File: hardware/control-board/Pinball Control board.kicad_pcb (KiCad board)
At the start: 2 copper layers, 87.1 x 100 mm, 108 parts, among them J1 Connector C, J3 B4B-XH-A, J4 Conn_01x10_Pin, J5 Conn_01x10_Pin, Q1 BSS138, Q10 BSS84, Q11 BSS138, Q12 BSS84, Q13 BSS138, Q14 BSS84, Q15 BSS138, Q16 IRFR5410, Q17 IRFR5410, Q18 IRFR5410, Q19 IRFR5410, Q2 BSS138, Q20 IRFR5410, Q3 BSS138, Q4 BSS138, Q5 BSS138, Q6 BSS84, Q7 BSS138, Q8 BSS84, Q9 BSS138, SW1 test switch, SW2 test switch

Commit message: Save routed board checkpoint and order checklist
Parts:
- removed C22, C23: 100nF, PCM_JLCPCB:C_0805
- removed the D10 at (136.1, 62.6)
- removed the D15 at (146.3, 132.8)
- removed the D16 at (136.2, 135.0)
- removed the D9 at (146.8, 59.6)
- removed Q1, Q11, Q13, Q15, Q2, Q3, Q4, Q5, Q7, Q9: BSS138, PCM_JLCPCB:Q_SOT-23
- removed Q10, Q12, Q14, Q6, Q8: BSS84, PCM_JLCPCB:Q_SOT-23
- removed Q16, Q17, Q18, Q19, Q20: IRFR5410, Package_TO_SOT_SMD:TO-252-2
- removed the R20 at (157.2, 97.6)
- removed R25, R26, R27, R28: 56Ω, PCM_JLCPCB:R_0805
- removed R29, R30, R31, R32, R33: 10kΩ, PCM_JLCPCB:R_0805
- removed the R3 at (117.4, 121.1)
- removed R34, R37, R50, R51: 2.4kΩ, PCM_JLCPCB:R_0805
- added C17: 100nF, PCM_JLCPCB:C_0805, F.Cu at (151.9, 141.4)
- added C18: 100nF, PCM_JLCPCB:C_0805, F.Cu at (151.9, 86.8)
- added D13: Red, PCM_JLCPCB:D_0805, F.Cu at (146.7, 69.0)
- added D14: Red, PCM_JLCPCB:D_0805, F.Cu at (146.7, 105.4)
- added D19: US1M, PCM_JLCPCB:D_SMA, F.Cu at (149.1, 82.4)
- added D20: SMCJ30CA, PCM_JLCPCB:D_SMC, F.Cu at (139.0, 81.7)
- added R10: 220Ω, PCM_JLCPCB:R_0805, F.Cu at (154.6, 123.8)
- added R11: 220Ω, PCM_JLCPCB:R_0805, F.Cu at (154.5, 141.4)
- added R12: 220Ω, PCM_JLCPCB:R_0805, F.Cu at (154.5, 86.7)
- added R13: 220Ω, PCM_JLCPCB:R_0805, F.Cu at (157.1, 69.0)
- added R2: 4.7kΩ, PCM_JLCPCB:R_0805, F.Cu at (108.5, 118.0)
- added U1: TPS1H200AQDGNRQ1, Snapmagic_TI_TPS1H200A_Q1:SOP65P490X110-9N, F.Cu at (151.9, 115.4)
- added U2: TPS1H200AQDGNRQ1, Snapmagic_TI_TPS1H200A_Q1:SOP65P490X110-9N, F.Cu at (152.0, 132.9)
- added U3: TPS1H200AQDGNRQ1, Snapmagic_TI_TPS1H200A_Q1:SOP65P490X110-9N, F.Cu at (151.4, 78.0)
- added U4: TPS1H200AQDGNRQ1, Snapmagic_TI_TPS1H200A_Q1:SOP65P490X110-9N, F.Cu at (151.4, 60.4)
- added U5: TPS1H200AQDGNRQ1, Snapmagic_TI_TPS1H200A_Q1:SOP65P490X110-9N, F.Cu at (151.9, 96.5)
- D11: value US1M -> Red; footprint PCM_JLCPCB:D_SMA -> PCM_JLCPCB:D_0805
- D12: value SMCJ30CA -> Red; footprint PCM_JLCPCB:D_SMC -> PCM_JLCPCB:D_0805
- D21, D23: value Red -> US1M; footprint PCM_JLCPCB:D_0805 -> PCM_JLCPCB:D_SMA
- D22, D24: value Red -> SMCJ30CA; footprint PCM_JLCPCB:D_0805 -> PCM_JLCPCB:D_SMC
- R14: value 10kΩ -> 220Ω
- R15, R16, R17, R18, R19: value 10kΩ -> 1kΩ
- R21, R22, R23: value 10kΩ -> 2.4kΩ
- R24: value 56Ω -> 2.4kΩ
- moved D22 73.7 mm to (139.0, 63.2), turned to -90 degrees
- moved C19 67.9 mm to (151.9, 69.0), turned to -90 degrees
- moved D21 61.8 mm to (149.2, 64.6)
- moved D17 59.7 mm to (149.1, 137.2)
- moved D18 56.5 mm to (138.8, 136.9)
- moved R22 53.1 mm to (149.3, 86.7), turned to 90 degrees
- moved D24 50.4 mm to (139.0, 99.6), turned to -90 degrees
- moved R14 46.5 mm to (154.5, 105.4), turned to 90 degrees
- moved D11 44.8 mm to (146.6, 141.4), turned to 90 degrees
- moved R17 44.8 mm to (157.0, 86.7), turned to 90 degrees
- moved D23 43.1 mm to (149.0, 100.9)
- moved C20 41.7 mm to (151.9, 105.4), turned to -90 degrees
- moved R24 39.5 mm to (149.3, 105.4), turned to 90 degrees
- moved D10 39.0 mm to (146.6, 123.8), turned to 90 degrees
- moved R20 38.5 mm to (149.3, 123.8)
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- renumbered C2 to C1, C11 to C10, C1 to C11, C13 to C12, C12 to C13, C21 to C16, C3 to C2, C4 to C3, C5 to C4, C6 to C5, C7 to C6, C8 to C7, C9 to C8, C10 to C9, D25 to D10, D13 to D15, D14 to D16, D19 to D9, H4 to H3, H3 to H4, J4 to J2, J5 to J4, R2 to R1, R52 to R20, R4 to R3, R5 to R4, R6 to R5, R7 to R6, R1 to R7, R38 to R9
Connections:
- C16 pad 2: GND (matrix GND1) -> GND
- C19 pad 1: SD3 -> SD5
- C19 pad 2: GND (matrix GND1) -> GND
- C20 pad 1: SD5 -> SD6
- C20 pad 2: GND (matrix GND1) -> GND
- D10 pad 1: Net-(D25-Pad1) -> GND
- D10 pad 2: GND (matrix GND1) -> Net-(D10-Pad2)
- D11 pad 1: +22vdc -> GND
- D11 pad 2: SD6 -> Net-(D11-Pad2)
- D12 pad 1: GND (matrix GND1) -> GND
- D12 pad 2: SD6 -> Net-(D12-Pad2)
- D16 pad 1: GND (matrix GND1) -> GND
- D17 pad 2: SD4 -> SD3
- D18 pad 1: GND (matrix GND1) -> GND
- D18 pad 2: SD4 -> SD3
- D21 pad 1: Net-(D21-Pad1) -> +22vdc
- D21 pad 2: GND (matrix GND1) -> SD5
- D22 pad 1: Net-(D22-Pad1) -> GND
- D22 pad 2: GND (matrix GND1) -> SD5
- D23 pad 1: Net-(D23-Pad1) -> +22vdc
- D23 pad 2: GND (matrix GND1) -> SD6
- D24 pad 1: Net-(D24-Pad1) -> GND
- D24 pad 2: GND (matrix GND1) -> SD6
- R14 pad 1: GND (matrix GND1) -> S6
- R14 pad 2: S5 -> Net-(U5-IN)
- R15 pad 1: GND (matrix GND1) -> Net-(U1-CL)
- R15 pad 2: S6 -> GND
- R16 pad 1: GND (matrix GND1) -> Net-(U2-CL)
- R16 pad 2: S2 -> GND
- R17 pad 1: GND (matrix GND1) -> Net-(U3-CL)
- R17 pad 2: S3 -> GND
- R18 pad 1: GND (matrix GND1) -> Net-(U4-CL)
- R18 pad 2: S4 -> GND
- R19 pad 2: +22vdc -> GND
- R20 pad 1: Net-(D25-Pad1) -> Net-(D10-Pad2)
- R21 pad 1: Net-(Q10-G) -> Net-(D11-Pad2)
- R21 pad 2: +22vdc -> SD3
- R22 pad 1: Net-(Q12-G) -> Net-(D12-Pad2)
- R22 pad 2: +22vdc -> SD4
- R23 pad 2: +22vdc -> SD5
- R24 pad 2: Net-(Q16-G) -> SD6
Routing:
- net GND: track 144.5 -> 530.6 mm, vias 3 -> 8
- net GND (matrix GND1): track 446.7 -> 163.5 mm, vias 35 -> 7
- net +22vdc: track 271.2 -> 201.5 mm, vias 7 -> 5
- net Net-(Q12-G): track 22.0 -> 0.00 mm, vias 2 -> 0
- net +18vdc: track 30.5 -> 50.7 mm
- net Net-(Q2-D): track 15.9 -> 0.00 mm
- net SD3: track 77.9 -> 62.1 mm
- net Net-(U4-CL): track 0.00 -> 15.6 mm
- net Net-(U3-CL): track 0.00 -> 13.4 mm
- net SD2: track 77.9 -> 64.6 mm
- net Net-(Q10-G): track 11.4 -> 0.00 mm
- net Net-(U5-CL): track 21.3 -> 10.6 mm, vias 2 -> 0
- net Start: track 28.8 -> 39.4 mm
- net Net-(Q12-D): track 10.5 -> 0.00 mm
- net Net-(Q8-D): track 10.2 -> 0.00 mm
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- added copper zone on B.Cu, net GND
- added copper zone on F.Cu, net GND
- removed copper zone on B.Cu, net GND (matrix GND1)
- removed copper zone on F.Cu, net GND (matrix GND1)

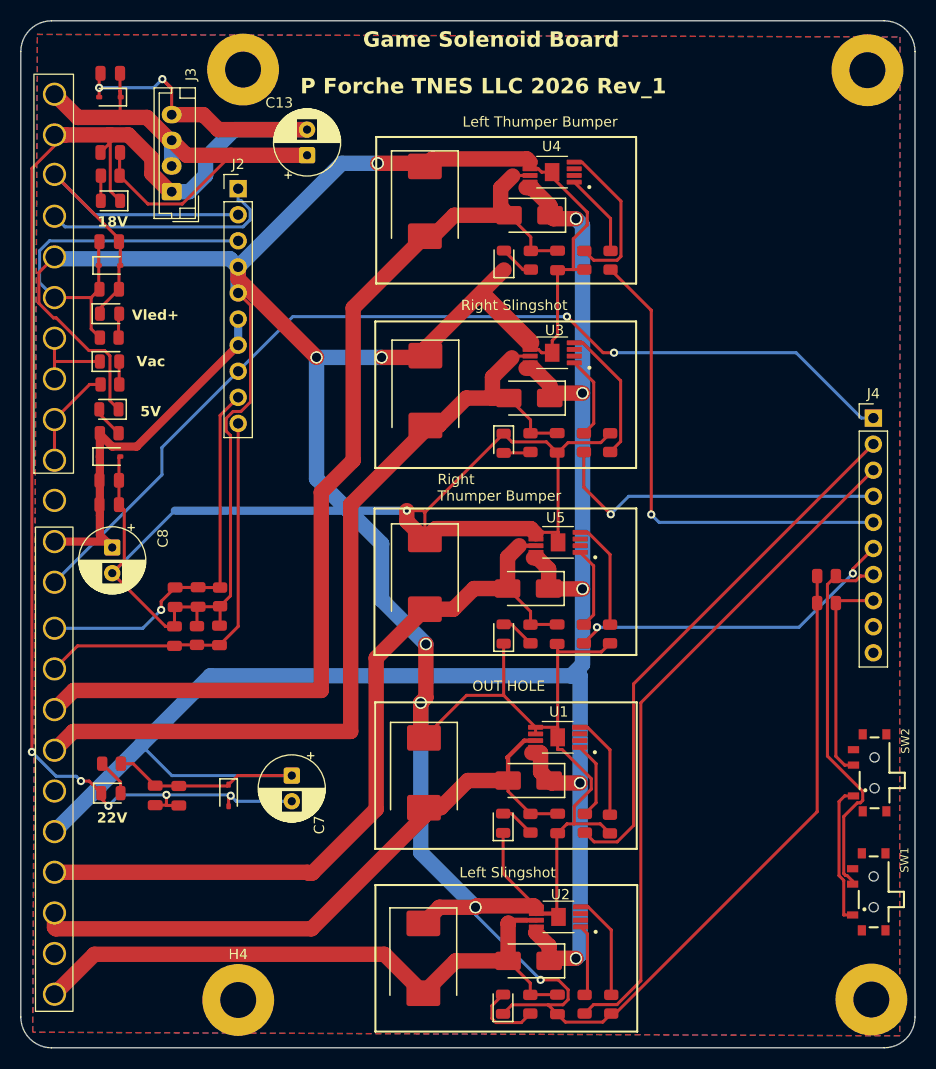
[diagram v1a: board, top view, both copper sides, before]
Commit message: Checkpoint KiCad schematic and PCB updates
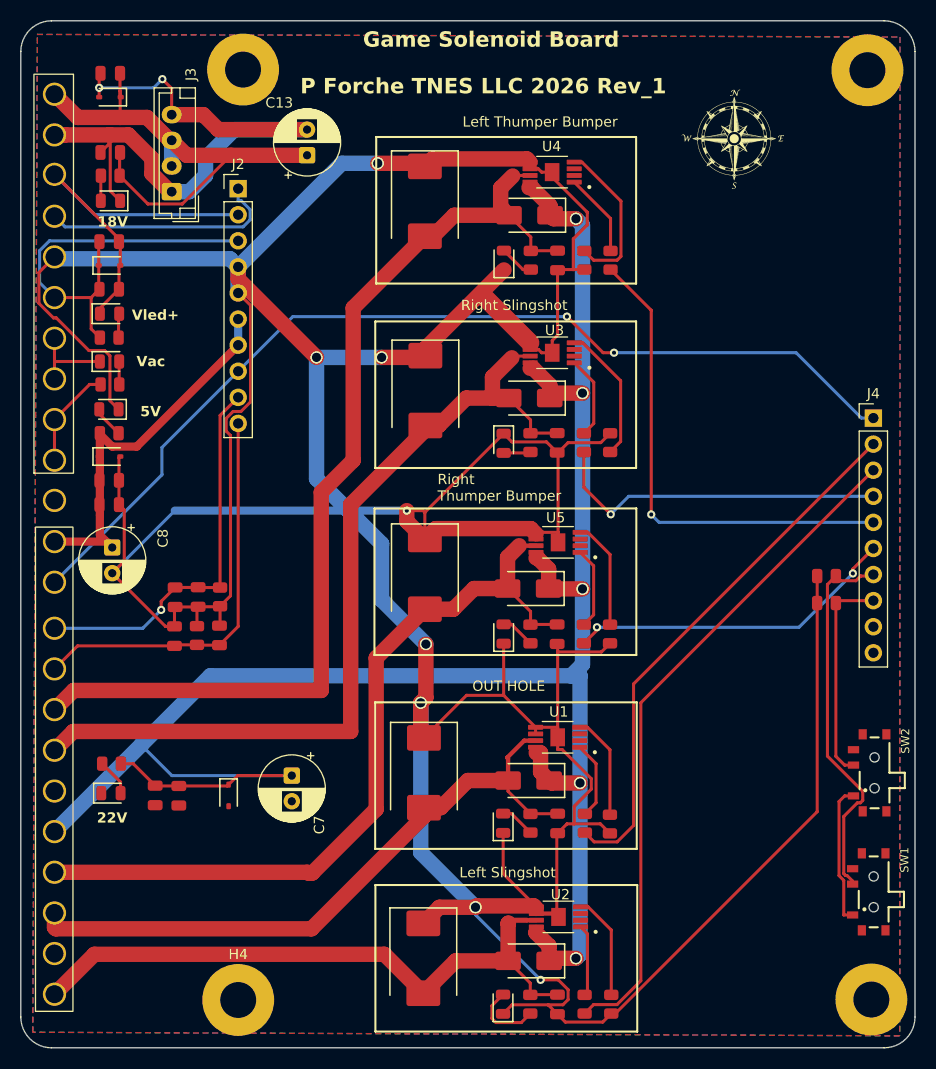
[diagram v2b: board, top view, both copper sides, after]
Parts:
- added 10mm1: ~, 1My_Parts_ Passive:10mm LOGO, F.Cu at (169.2, 57.1)
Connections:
- C1 pad 2: GND (matrix GND1) -> GND
- C3 pad 2: GND (matrix GND1) -> GND
- C7 pad 2: GND (matrix GND1) -> GND
- D2 pad 1: GND (matrix GND1) -> GND
- D3 pad 2: GND (matrix GND1) -> GND
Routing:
- net GND (matrix GND1): track 163.5 -> 66.6 mm, vias 7 -> 2
- net +22vdc: track 201.5 -> 200.1 mm
